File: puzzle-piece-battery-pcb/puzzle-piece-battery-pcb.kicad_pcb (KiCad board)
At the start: 2 copper layers, 27 x 27 mm, 2 parts, among them J2 INPUT, J3 OUTPUT

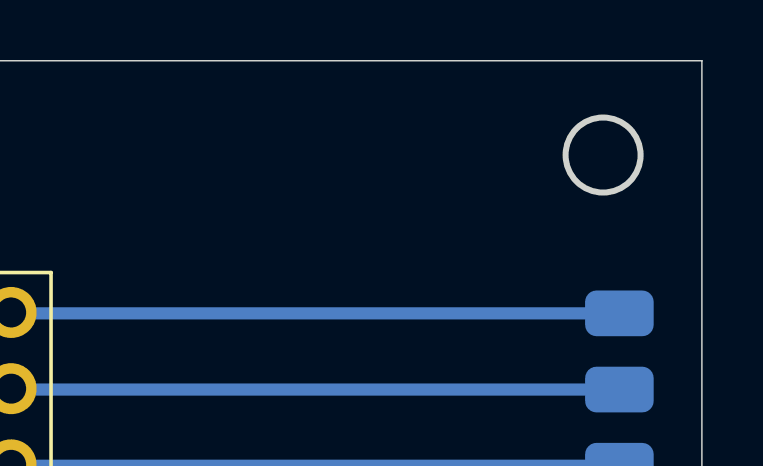
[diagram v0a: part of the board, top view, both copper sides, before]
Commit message: made puzzle-controller board double sided
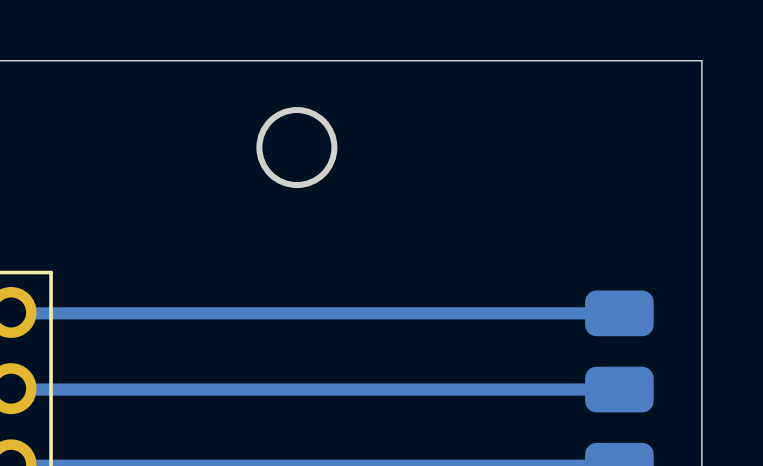
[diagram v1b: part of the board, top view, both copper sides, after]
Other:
- outline, holes or cut-outs redrawn
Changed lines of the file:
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@@
 	)
 	(gr_circle
-		(center 186.207 72.643)
-		(end 187.457 72.643)
+		(center 176 72.393)
+		(end 177.25 72.393)
 		(stroke
 			(width 0.2)
@@
 		)
 		(height -0.5)
-		(gr_text "1062.9921 mils"
+		(gr_text "27.0000 mm"
 			(at 176 67.7 0)
 			(layer "F.SilkS")
@@
 		)
 		(height 0)
-		(gr_text "1062.9921 mils"
+		(gr_text "27.0000 mm"
 			(at 160.7 83 90)
 			(layer "F.SilkS")

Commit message: current puzzle with attiny and pogo pins
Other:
- board size 27 x 27 mm -> 29.2 x 29.2 mm
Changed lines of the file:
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@@
 	)
 	(gr_circle
-		(center 165.793 93.357)
-		(end 167.043 93.357)
+		(center 162.5 96.5)
+		(end 162.5 97.6)
 		(stroke
-			(width 0.2)
-			(type default)
-		)
-		(fill none)
-		(layer "Edge.Cuts")
-	)
-	(gr_circle
-		(center 176 72.393)
-		(end 177.25 72.393)
-		(stroke
-			(width 0.2)
+			(width 0.05)
 			(type default)
 		)
@@
 		(stroke
 			(width 0.05)
+			(type default)
+		)
+		(fill none)
+		(layer "Edge.Cuts")
+	)
+	(gr_circle
+		(center 189.5 69.5)
+		(end 190.6 69.5)
+		(stroke
+			(width 0.05)
